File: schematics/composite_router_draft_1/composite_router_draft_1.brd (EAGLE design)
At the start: 100 x 80 mm, 44 parts, among them U1 ARDUINO-MEGA

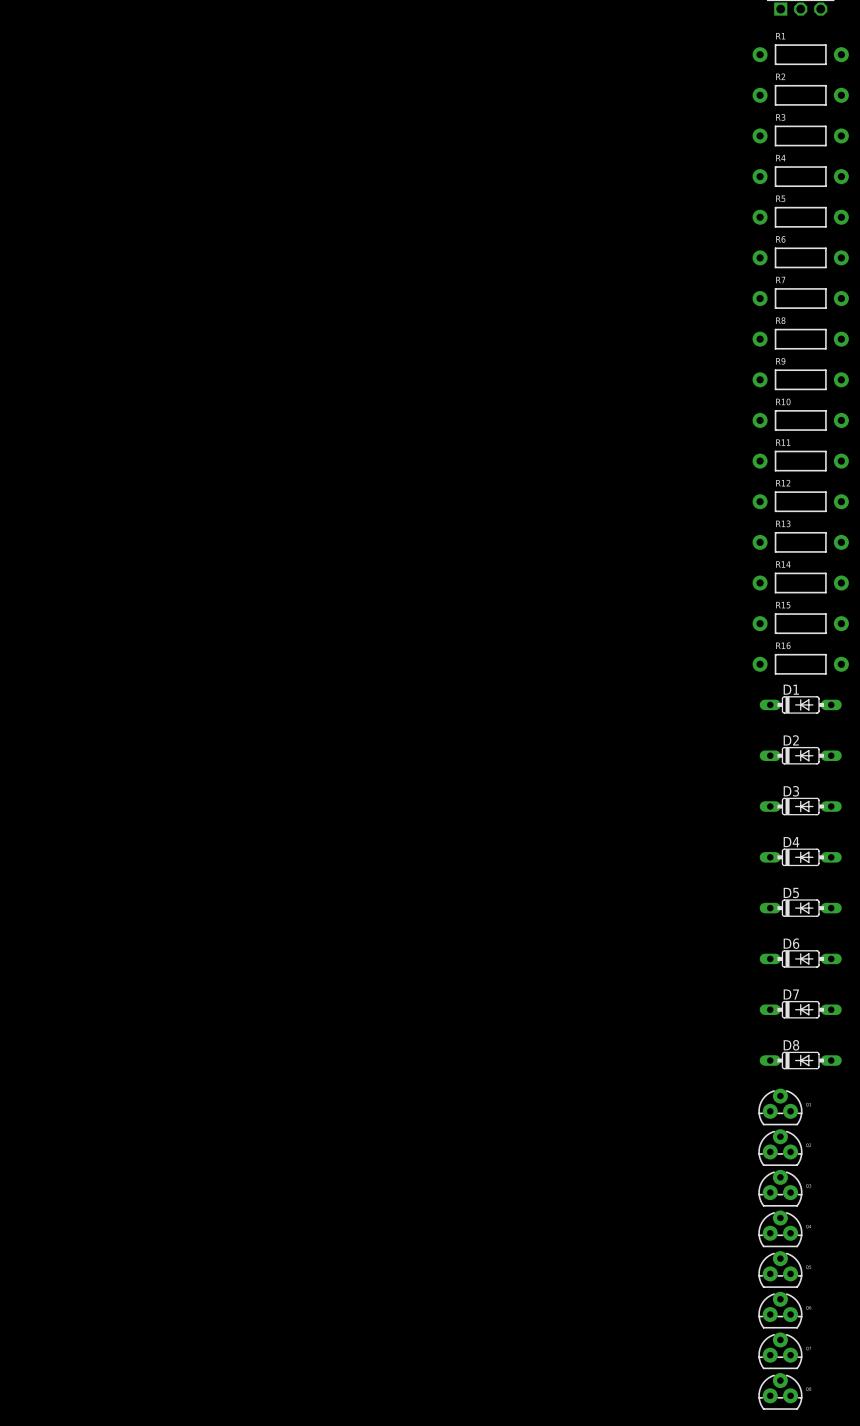
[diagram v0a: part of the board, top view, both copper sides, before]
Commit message: tested arduino relay
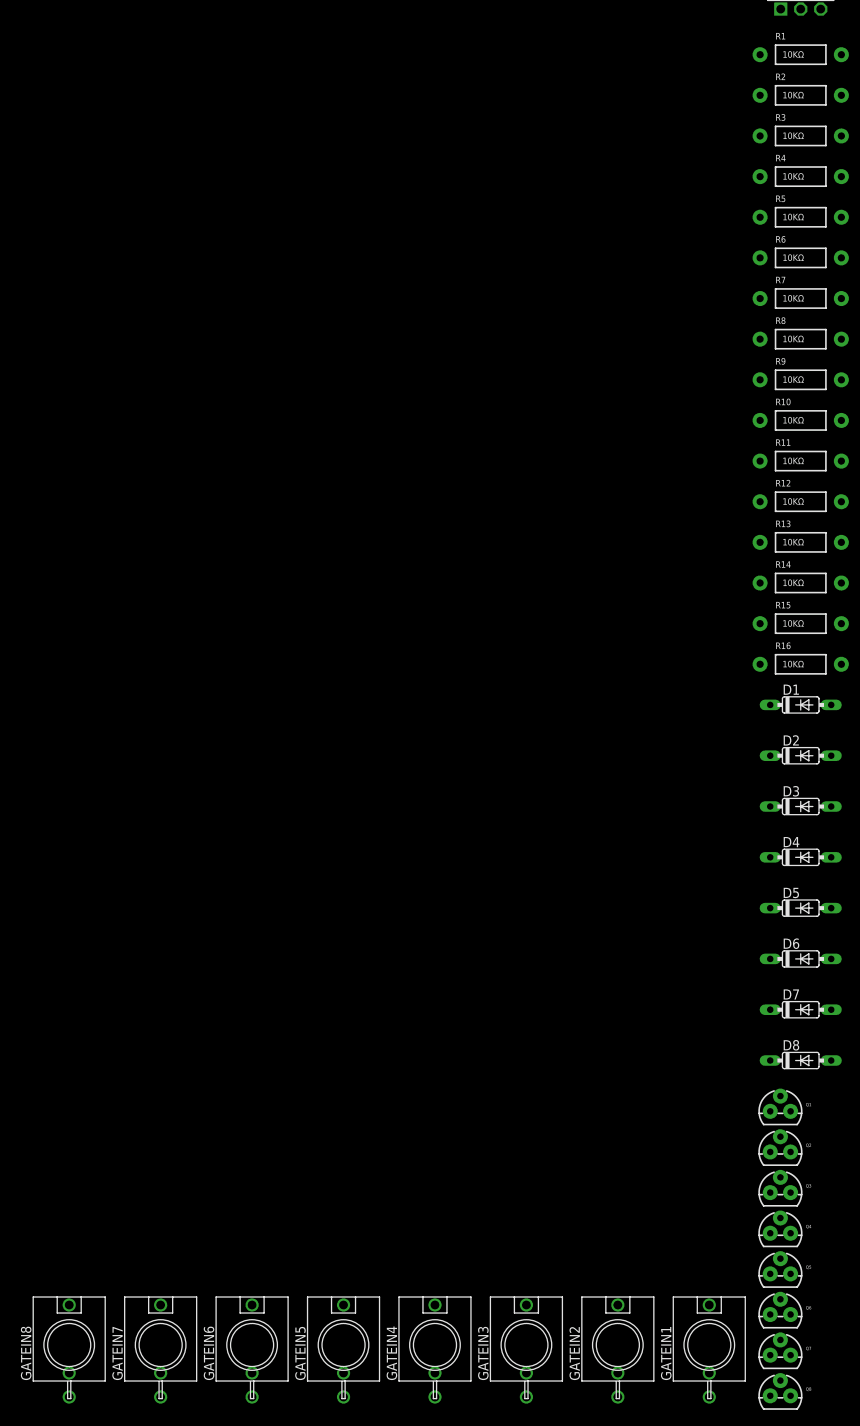
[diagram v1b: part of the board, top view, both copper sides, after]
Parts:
- added GATEIN1, GATEIN2, GATEIN3, GATEIN4, GATEIN5, GATEIN6, GATEIN7, GATEIN8: THONKICONNNEW, MusicThingModular:WQP-PJ301M-12_JACK
- R1, R10, R11, R12, R13, R14, R15, R16, R2, R3, R4, R5, R6, R7, R8, R9: value (none) -> 10KΩ
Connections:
- new net N$25: GATEIN1.P$1_TIP, R1.P$1
- new net N$34: D1.C, Q1.2, R1.P$2
- new net N$35: GATEIN3.P$1_TIP, R5.P$1
- new net N$36: D3.C, Q3.2, R5.P$2
- new net N$37: Q1.3, R2.P$1
- new net N$38: D2.C, Q2.2, R3.P$2
- new net N$39: Q2.3, R4.P$2
- new net N$40: GATEIN2.P$1_TIP, R3.P$1
- new net N$41: Q3.3, R6.P$1
- new net N$44: GATEIN4.P$1_TIP, R7.P$1
- new net N$45: D4.C, Q4.2, R7.P$2
- new net N$46: Q4.3, R8.P$1
- new net N$48: GATEIN5.P$1_TIP, R9.P$1
- new net N$49: D5.C, Q5.2, R9.P$2
- new net N$50: Q5.3, R10.P$1
- new net N$53: GATEIN6.P$1_TIP, R11.P$1
- new net N$54: D6.C, Q6.2, R11.P$2
- new net N$55: Q6.3, R12.P$1
- new net N$56: D6.A, Q6.1
- net GND: now also D1.A, D2.A, D3.A, D4.A, D5.A, GATEIN1.P$3_SLEEVE, GATEIN2.P$3_SLEEVE, GATEIN3.P$3_SLEEVE, GATEIN4.P$3_SLEEVE, GATEIN5.P$3_SLEEVE, Q1.1, Q2.1, Q3.1, Q4.1, Q5.1
- net VCC: now also R10.P$2, R12.P$2, R2.P$2, R4.P$1, R8.P$2
